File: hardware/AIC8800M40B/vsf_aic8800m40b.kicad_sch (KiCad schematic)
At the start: 86 parts, among them J1 USB_A, J2 USB_C_Receptacle_USB2.0, J3 USB_C_Receptacle_USB2.0, J4 Micro_SD_Card_Det1, J6 Conn_Coaxial, J7 Conn_Coaxial, J8 Conn_02x15_Odd_Even, Q1 S9013, SW1 SW_Push, SW2 SW_Push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

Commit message: [hardware/aic8800m40b] update LED footprint to 0603
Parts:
- D5: footprint LED_SMD:LED_0402_1005Metric -> LED_SMD:LED_0603_1608Metric
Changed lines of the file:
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@@
       (effects (font (size 1.27 1.27)))
     )
-    (property "Footprint" "LED_SMD:LED_0402_1005Metric" (at 267.97 27.94 0)
+    (property "Footprint" "LED_SMD:LED_0603_1608Metric" (at 267.97 27.94 0)
       (effects (font (size 1.27 1.27)) hide)
     )

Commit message: [hardware/aic8800m40b] update
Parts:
- R25: value 10k -> 4.7k
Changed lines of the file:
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@@
       (effects (font (size 1.27 1.27)))
     )
-    (property "Value" "10k" (at 201.93 143.51 90)
+    (property "Value" "4.7k" (at 201.93 143.51 90)
       (effects (font (size 1.27 1.27)))
     )

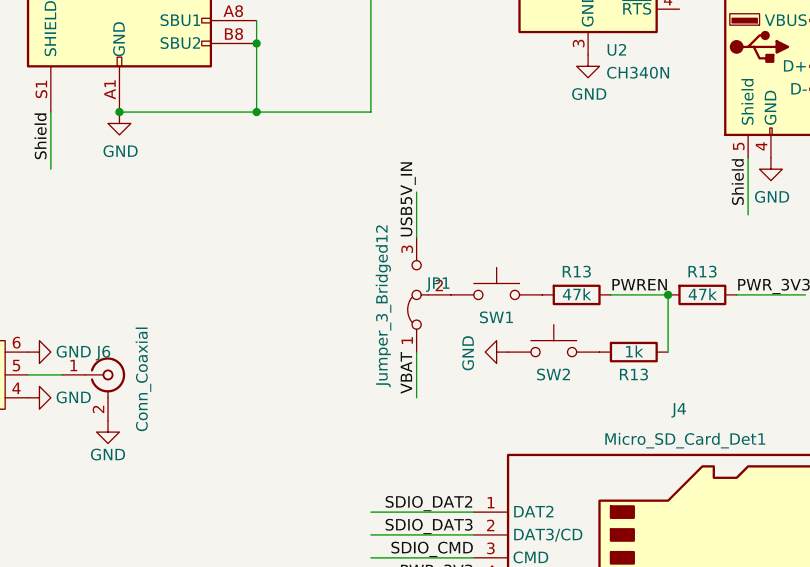
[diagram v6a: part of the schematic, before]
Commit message: [hardware/aic8800m40b] leave J2 open
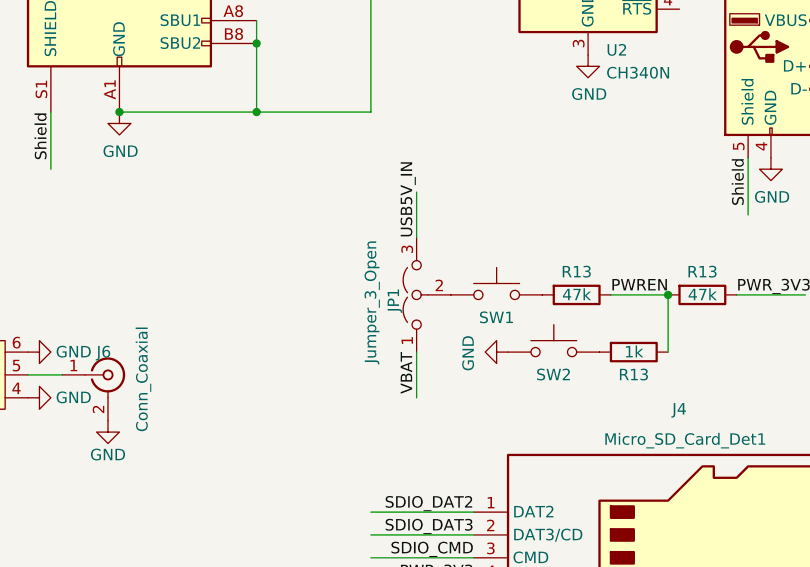
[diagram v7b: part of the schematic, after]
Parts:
- removed JP1: Jumper_3_Bridged12, Jumper:SolderJumper-3_P1.3mm_Bridged12_RoundedPad1.0x1.5mm_NumberLabels, symbol Jumper:Jumper_3_Bridged12
- added JP1: Jumper_3_Open, Jumper:SolderJumper-3_P1.3mm_Open_RoundedPad1.0x1.5mm_NumberLabels, symbol Jumper:Jumper_3_Open
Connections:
- net USB5V_IN: now also JP1.3 (B)
- net VBAT: now also JP1.1 (A)
- net at SW1.1: now also JP1.2 (C)
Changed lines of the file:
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@@
     (effects (font (size 1.27 1.27)) (justify left bottom))
+  )
+  (symbol (lib_id "Jumper:Jumper_3_Open") (at 158.75 80.01 90) (unit 1)
+    (in_bom yes) (on_board yes) (dnp no)
+    (property "Reference" "JP1" (at 156.21 81.915 0)
+      (effects (font (size 1.27 1.27)) (justify left))
+    )
+    (property "Value" "Jumper_3_Open" (at 153.67 87.63 0)
+      (effects (font (size 1.27 1.27)) (justify left))
+    )
+    (property "Footprint" "Jumper:SolderJumper-3_P1.3mm_Open_RoundedPad1.0x1.5mm_NumberLabels" (at 158.75 80.01 0)
+      (effects (font (size 1.27 1.27)) hide)
+    )
+    (property "Datasheet" "~" (at 158.75 80.01 0)
+      (effects (font (size 1.27 1.27)) hide)
+    )
+    (pin "1")
+    (pin "2")
+    (pin "3")
+    (instances
+      (project "vsf_aic8800m40b"
+        (path "/7ff897c7-5676-47e3-800e-188ea4d80e23"
+          (reference "JP1") (unit 1)
+        )
+      )
+    )
   )
   (symbol (lib_id "Device:C") (at 100.33 82.55 0) (unit 1)
@@
         )
       )
-    )
-  )
-  (symbol (lib_id "Jumper:Jumper_3_Bridged12") (at 158.75 80.01 90) (unit 1)
-    (in_bom yes) (on_board yes) (dnp no)
-    (property "Reference" "JP1" (at 162.56 78.74 90)
-      (effects (font (size 1.27 1.27)) (justify left))
-    )
-    (property "Value" "Jumper_3_Bridged12" (at 154.94 90.17 0)
-      (effects (font (size 1.27 1.27)) (justify left))
-    )
-    (property "Footprint" "Jumper:SolderJumper-3_P1.3mm_Bridged12_RoundedPad1.0x1.5mm_NumberLabels" (at 158.75 80.01 0)
-      (effects (font (size 1.27 1.27)) hide)
-    )
-    (property "Datasheet" "~" (at 158.75 80.01 0)
-      (effects (font (size 1.27 1.27)) hide)
-    )
-    (pin "1")
-    (pin "2")
-    (pin "3")
-    (instances
-      (project "vsf_aic8800m40b"
-        (path "/7ff897c7-5676-47e3-800e-188ea4d80e23"
-          (reference "JP1") (unit 1)
-        )
-      )
-      (project "MCULinux"
-        (path "/b0717bb8-5e5d-44de-b48f-ff278896fb50"
-          (reference "JP1") (unit 1)
-        )
-      )

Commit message: [hardware/aic8800m40b] update
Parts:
- removed JP1: Jumper_3_Open, Jumper:SolderJumper-3_P1.3mm_Open_RoundedPad1.0x1.5mm_NumberLabels, symbol Jumper:Jumper_3_Open
- added JP1, JP2: Jumper_2_Open, VSF:SolderJumper-2_P0.8mm_Open_Pad0.6x0.8mm, symbol Jumper:Jumper_2_Open
- R8, R9: value 22 -> 0
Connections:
- net USB5V_IN: now also JP1.1 (A), JP2.1 (A); no longer C3.1, U3.1 (VIN)
- net USB5V_OUT: now also JP1.2 (B)
- net VBAT: now also SW1.1
- new net: C3.1, JP2.2 (B), U3.1 (VIN)
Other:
- moved on the sheet: R13, SW1, SW2
